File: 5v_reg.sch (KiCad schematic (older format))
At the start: 2 parts

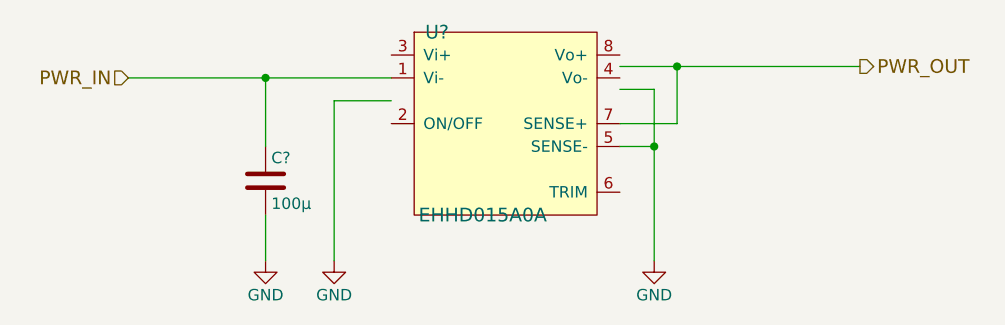
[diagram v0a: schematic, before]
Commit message: add 5v power switch
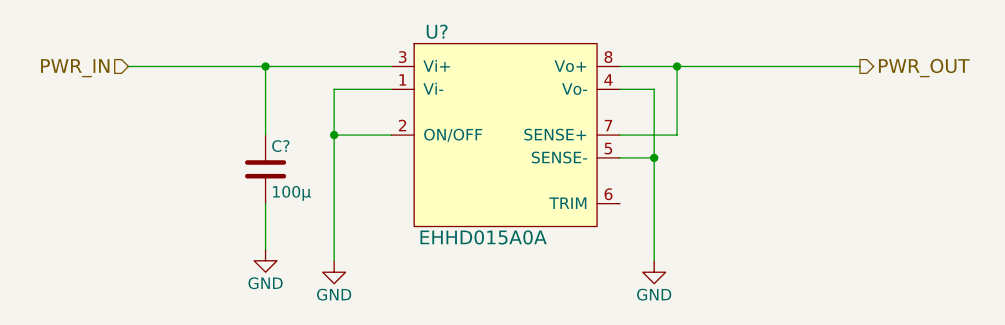
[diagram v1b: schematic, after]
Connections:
- wire segments 14 -> 12
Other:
- moved on the sheet: C?, U?
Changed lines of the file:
@@
 $Descr A4 11693 8268
 encoding utf-8
-Sheet 3 6
+Sheet 3 7
 Title "5V Regulator"
 Date "2017-07-02"
@@
 L EHHD015A0A U?
 U 1 1 595CAEC9
-P 6100 3750
-F 0 "U?" H 5800 4150 60  0000 C CNN
+P 6100 3800
+F 0 "U?" H 5800 4250 60  0000 C CNN
 F 1 "EHHD015A0A" H 6000 3350 60  0000 C CNN
-F 2 "" H 5800 3700 60  0001 C CNN
-F 3 "" H 5800 3700 60  0001 C CNN
-	1    6100 3750
+F 2 "" H 5800 3750 60  0001 C CNN
+F 3 "" H 5800 3750 60  0001 C CNN
+	1    6100 3800
 	1    0    0    -1
 $EndComp
 Wire Wire Line
-	4450 3550 5050 3550
+	4450 3500 5600 3500
 Wire Wire Line
-	5050 3550 5600 3550
+	5350 3600 5350 4350
 Wire Wire Line
-	5350 4350 5350 3650
-Wire Wire Line
-	5350 3650 5600 3650
+	5350 3800 5600 3800
 $Comp
 L GND #PWR?
@@
 L C C?
 U 1 1 595CAFFF
-P 5050 4000
-F 0 "C?" H 5075 4100 50  0000 L CNN
-F 1 "100μ" H 5075 3900 50  0000 L CNN
-F 2 "" H 5088 3850 50  0001 C CNN
-F 3 "" H 5050 4000 50  0001 C CNN
-	1    5050 4000
+P 5050 3950
+F 0 "C?" H 5075 4050 50  0000 L CNN
+F 1 "100μ" H 5075 3850 50  0000 L CNN
+F 2 "" H 5088 3800 50  0001 C CNN
+F 3 "" H 5050 3950 50  0001 C CNN
+	1    5050 3950
 	1    0    0    -1
 $EndComp
@@
 L GND #PWR?
 U 1 1 595CB07E
-P 5050 4350
-F 0 "#PWR?" H 5050 4100 50  0001 C CNN
-F 1 "GND" H 5050 4200 50  0000 C CNN
-F 2 "" H 5050 4350 50  0001 C CNN
-F 3 "" H 5050 4350 50  0001 C CNN
-	1    5050 4350
+P 5050 4300
+F 0 "#PWR?" H 5050 4050 50  0001 C CNN
+F 1 "GND" H 5050 4150 50  0000 C CNN
+F 2 "" H 5050 4300 50  0001 C CNN
+F 3 "" H 5050 4300 50  0001 C CNN
+	1    5050 4300
 	1    0    0    -1
 $EndComp
 Wire Wire Line
-	5050 4150 5050 4350
+	5050 4100 5050 4300
 Wire Wire Line
-	5050 3850 5050 3550
-Connection ~ 5050 3550
+	5050 3800 5050 3500
+Connection ~ 5050 3500
 Wire Wire Line
-	6600 3500 6850 3500
+	6600 3500 7650 3500
 Wire Wire Line
-	6850 3500 7650 3500
+	6600 3800 6850 3800
 Wire Wire Line
-	6600 3750 6850 3750
-Wire Wire Line
-	6850 3750 6850 3500
+	6850 3800 6850 3500
 Connection ~ 6850 3500
 Wire Wire Line
 	6600 3600 6750 3600
 Wire Wire Line
-	6750 3600 6750 3850
+	6750 3600 6750 4350
 Wire Wire Line
-	6750 3850 6750 4350
-Wire Wire Line
-	6600 3850 6750 3850
-Connection ~ 6750 3850
+	6600 3900 6750 3900
+Connection ~ 6750 3900
 $Comp
 L GND #PWR?
@@
 	1    0    0    -1
 $EndComp
-Text HLabel 4450 3550 0    60   Input ~ 0
+Text HLabel 4450 3500 0    60   Input ~ 0
 PWR_IN
 Text HLabel 7650 3500 2    60   Output ~ 0
 PWR_OUT
+Wire Wire Line
+	5600 3600 5350 3600
+Connection ~ 5350 3800
 $EndSCHEMATC

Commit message: clean up after annotate
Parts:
- gave numbers to parts that had none: 2
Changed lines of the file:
@@
 $EndDescr
 $Comp
-L EHHD015A0A U?
+L EHHD015A0A U2
 U 1 1 595CAEC9
 P 6100 3800
-F 0 "U?" H 5800 4250 60  0000 C CNN
+F 0 "U2" H 5800 4250 60  0000 C CNN
 F 1 "EHHD015A0A" H 6000 3350 60  0000 C CNN
 F 2 "" H 5800 3750 60  0001 C CNN
@@
 $EndComp
 Wire Wire Line
-	4450 3500 5600 3500
+	4450 3500 5050 3500
 Wire Wire Line
-	5350 3600 5350 4350
+	5050 3500 5600 3500
+Wire Wire Line
+	5350 3600 5350 3800
+Wire Wire Line
+	5350 3800 5350 4350
 Wire Wire Line
 	5350 3800 5600 3800
 $Comp
-L GND #PWR?
+L GND #PWR10
 U 1 1 595CAFE9
 P 5350 4350
-F 0 "#PWR?" H 5350 4100 50  0001 C CNN
+F 0 "#PWR10" H 5350 4100 50  0001 C CNN
 F 1 "GND" H 5350 4200 50  0000 C CNN
 F 2 "" H 5350 4350 50  0001 C CNN
@@
 $EndComp
 $Comp
-L C C?
+L C C4
 U 1 1 595CAFFF
 P 5050 3950
-F 0 "C?" H 5075 4050 50  0000 L CNN
+F 0 "C4" H 5075 4050 50  0000 L CNN
 F 1 "100μ" H 5075 3850 50  0000 L CNN
 F 2 "" H 5088 3800 50  0001 C CNN
@@
 $EndComp
 $Comp
-L GND #PWR?
+L GND #PWR9
 U 1 1 595CB07E
-P 5050 4300
-F 0 "#PWR?" H 5050 4050 50  0001 C CNN
-F 1 "GND" H 5050 4150 50  0000 C CNN
-F 2 "" H 5050 4300 50  0001 C CNN
-F 3 "" H 5050 4300 50  0001 C CNN
-	1    5050 4300
+P 5050 4350
+F 0 "#PWR9" H 5050 4100 50  0001 C CNN
+F 1 "GND" H 5050 4200 50  0000 C CNN
+F 2 "" H 5050 4350 50  0001 C CNN
+F 3 "" H 5050 4350 50  0001 C CNN
+	1    5050 4350
 	1    0    0    -1
 $EndComp
 Wire Wire Line
-	5050 4100 5050 4300
+	5050 4100 5050 4350
 Wire Wire Line
 	5050 3800 5050 3500
 Connection ~ 5050 3500
 Wire Wire Line
-	6600 3500 7650 3500
+	6600 3500 6850 3500
+Wire Wire Line
+	6850 3500 7650 3500
 Wire Wire Line
 	6600 3800 6850 3800
@@
 	6600 3600 6750 3600
 Wire Wire Line
-	6750 3600 6750 4350
+	6750 3600 6750 3900
+Wire Wire Line
+	6750 3900 6750 4350
 Wire Wire Line
 	6600 3900 6750 3900
 Connection ~ 6750 3900
 $Comp
-L GND #PWR?
+L GND #PWR11
 U 1 1 595CB277
 P 6750 4350
-F 0 "#PWR?" H 6750 4100 50  0001 C CNN
+F 0 "#PWR11" H 6750 4100 50  0001 C CNN
 F 1 "GND" H 6750 4200 50  0000 C CNN
 F 2 "" H 6750 4350 50  0001 C CNN

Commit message: fix issue with incorrect symbol
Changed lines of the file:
@@
 $EndComp
 Wire Wire Line
-	4450 3500 5050 3500
+	4450 3500 5600 3500
 Wire Wire Line
-	5050 3500 5600 3500
-Wire Wire Line
-	5350 3600 5350 3800
-Wire Wire Line
-	5350 3800 5350 4350
+	5350 3600 5350 4350
 Wire Wire Line
 	5350 3800 5600 3800
 $Comp
-L GND #PWR10
+L GND #PWR09
 U 1 1 595CAFE9
 P 5350 4350
-F 0 "#PWR10" H 5350 4100 50  0001 C CNN
+F 0 "#PWR09" H 5350 4100 50  0001 C CNN
 F 1 "GND" H 5350 4200 50  0000 C CNN
 F 2 "" H 5350 4350 50  0001 C CNN
@@
 $EndComp
 $Comp
-L GND #PWR9
+L GND #PWR010
 U 1 1 595CB07E
 P 5050 4350
-F 0 "#PWR9" H 5050 4100 50  0001 C CNN
+F 0 "#PWR010" H 5050 4100 50  0001 C CNN
 F 1 "GND" H 5050 4200 50  0000 C CNN
 F 2 "" H 5050 4350 50  0001 C CNN
@@
 Connection ~ 5050 3500
 Wire Wire Line
-	6600 3500 6850 3500
-Wire Wire Line
-	6850 3500 7650 3500
+	6600 3500 7650 3500
 Wire Wire Line
 	6600 3800 6850 3800
@@
 	6600 3600 6750 3600
 Wire Wire Line
-	6750 3600 6750 3900
-Wire Wire Line
-	6750 3900 6750 4350
+	6750 3600 6750 4350
 Wire Wire Line
 	6600 3900 6750 3900
 Connection ~ 6750 3900
 $Comp
-L GND #PWR11
+L GND #PWR011
 U 1 1 595CB277
 P 6750 4350
-F 0 "#PWR11" H 6750 4100 50  0001 C CNN
+F 0 "#PWR011" H 6750 4100 50  0001 C CNN
 F 1 "GND" H 6750 4200 50  0000 C CNN
 F 2 "" H 6750 4350 50  0001 C CNN
